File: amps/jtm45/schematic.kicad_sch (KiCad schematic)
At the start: 62 parts, among them T3 OT

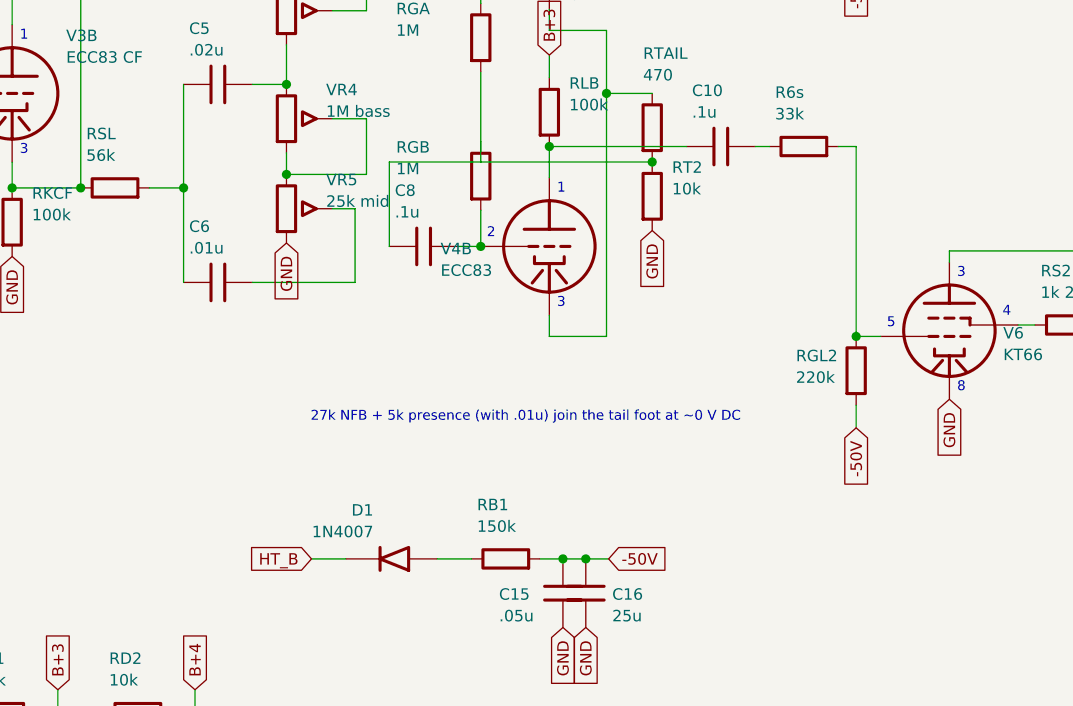
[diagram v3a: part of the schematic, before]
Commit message: Correct Marshall tail returns, tone values and source explanations (#34)
* Fix JTM45 tail return and source-read tone capacitor assignments

Read jtm45tr.gif at 2194x1539: PI/tone crop (1080,250)-(1490,675) shows the 10k tail ending at the feedback/presence junction, bass .01u and middle .02u. Model and draw both DC returns, label the presence parts, reconcile the derived board and retire the incorrect KPI dispute. All twelve chart nodes now pass; KPI 43.048 V vs 40 V, worst deviation 9.7%.

Correct the excluded tremolo description from bias modulation to the V2-driven 2G374 signal shunt; retain the plain head scope. Source: https://www.drtube.com/schematics/marshall/jtm45tr.gif. Both board styles and schematic preview inspected; KiCanvas review remains required at integration.

Signed-off-by: AnalogMaker <theanalogmaker@gmail.com>

* Include JTM100 feedback resistor as a second DC tail return

The 1068x759 factory 1959t-66.gif crop (475,160)-(775,500) shows 27k from the presence junction through the OT secondary, parallel with the 5k track. It is not DC-neutral. Adding RNFB brings PRES from18.092 to15.352 V (chart16) and KPI from55.978 to53.452 V (chart52), with no drawing or claim changes. Correct the explanation and its outdated JTM45 comparison.

Source: https://www.drtube.com/schematics/marshall/1959t-66.gif
Signed-off-by: AnalogMaker <theanalogmaker@gmail.com>

* Restore M1959 presence track and separate feedback tail node

Read Unicord70-6-11 revB from native1377x904 embedded page3 of the cited PDF. Crop(770,165)-(1030,490) grounds the 5k lower lug; 47k feedback and the cold-grid .1u coupler share the tail foot after10k. Crop(1230,210)-(1360,325) resolves feedback at8 ohms, hopping the16-ohm lead. Reconcile model, sheet, board, BOM and prose.

The page2 Mark II drawing has a different4.7k/DC-blocked presence return. Remove the false identical-front-end and chart-proves-grounded-tail claims, retain the printed18.5 V value and report the36.502 V simulation hone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
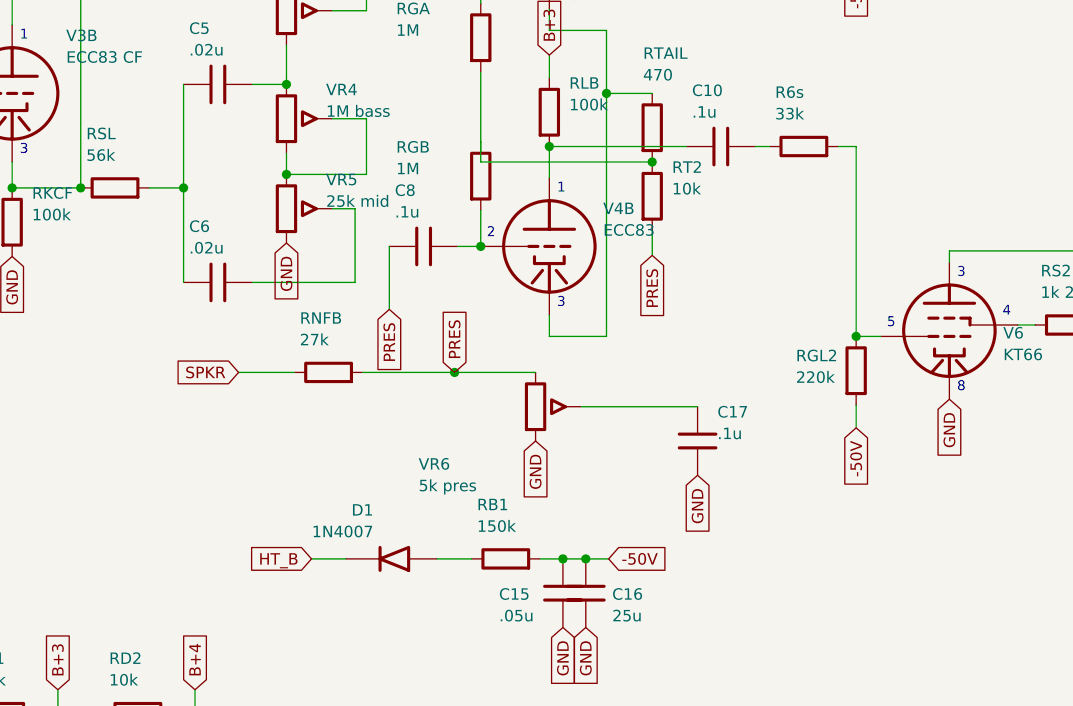
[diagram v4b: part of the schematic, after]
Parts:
- removed C11: 32u, symbol cx:C
- removed C13, C14: 16u, symbol cx:C
- removed RGB: 1M, symbol cx:R
- removed RGL1: 220k, symbol cx:R
- removed RS1: 1k 2W, symbol cx:R
- added C15: .05u, symbol cx:C
- added C17, C8, C9: .1u, symbol cx:C
- added D1: 1N4007, symbol cx:DIODE_SS
- added R6s: 33k, symbol cx:R
- added RB1: 150k, symbol cx:R
- added V6: KT66, symbol cx:PENTODE
- added VR6: 5k pres, symbol cx:POT
- C11: renamed from C12; value 16u -> 32u
- C12: renamed from RD2; value 10k -> 16u; symbol cx:R -> cx:C
- C13: renamed from D1; value 1N4007 -> 16u; symbol cx:DIODE_SS -> cx:C
- C14: renamed from C15; value .05u -> 16u
- C6: value .01u -> .02u
- RD2: renamed from RB1; value 150k -> 10k
- RGB: renamed from C8; value .1u -> 1M; symbol cx:C -> cx:R
- RGL1: renamed from R6s; value 33k -> 220k
- RNFB: renamed from C9; value .1u -> 27k; symbol cx:C -> cx:R
- RS1: renamed from V6; value KT66 -> 1k 2W; symbol cx:PENTODE -> cx:R
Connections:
- net -50V: now also RGL1.2, C15.1, RB1.2; no longer C14.1, RD2.2
- net B+1: now also C11.1
- net B+2: now also C12.1, RS1.2; no longer C11.1
- net B+3: now also C13.1, RD2.1; no longer C12.1
- net B+4: now also C14.1, RD2.2; no longer C12.2
- net GND: now also C12.2, C13.2, C15.2, C17.2, V6.4 (K), VR6.3; no longer RS1.4 (K), RT2.2
- net HT_B: now also D1.2 (K); no longer C13.2 (K)
- net SPKR: now also RNFB.1
- net at RS2.1: now also V6.3 (G2); no longer RS1.3 (G2)
- net at RGB.2, V4B.2 (G): now also C8.2
- net at R5s.2, V5.2 (G1): now also RGL1.1
- net at C10.2: now also R6s.1; no longer RGL1.1
- net at V5.3 (G2): now also RS1.1
- net at RLA.2, V4A.1 (P): now also C9.1; no longer RNFB.1
- net at R5s.1: now also C9.2; no longer RNFB.2
- net at T3.3 (PRI_B): now also V6.1 (P); no longer RS1.1 (P)
- new net: D1.1 (A), RB1.1
- new net: R6s.2, RGL2.1, V6.2 (G1)
- new net: C17.1, VR6.2 (W)
- new net PRES: C8.1, RNFB.2, RT2.2, VR6.1
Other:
- note removed: "27k NFB + 5k presence (with .01u) join the tail foot at ~0 V DC"
- moved on the sheet: C11, C13, C14, RD2, RGL1
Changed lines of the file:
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@@
     (in_bom yes) (on_board yes)
     (property "Reference" "C6" (at 130.109 70.078 270) (effects (font (size 1.27 1.27)) (justify left)))
-    (property "Value" ".01u" (at 130.109 72.478 270) (effects (font (size 1.27 1.27)) (justify left))))
+    (property "Value" ".02u" (at 130.109 72.478 270) (effects (font (size 1.27 1.27)) (justify left))))
   (wire (pts (xy 129.499 76.278) (xy 129.499 76.278))
     (stroke (width 0) (type default)))
@@
   (symbol (lib_id "cx:TRIODE") (at 170.139 72.278 0) (unit 1)
     (in_bom yes) (on_board yes)
-    (property "Reference" "V4B" (at 158.051 72.558 0) (effects (font (size 1.27 1.27)) (justify left)))
-    (property "Value" "ECC83" (at 158.051 74.958 0) (effects (font (size 1.27 1.27)) (justify left))))
+    (property "Reference" "V4B" (at 176.119 68.098 0) (effects (font (size 1.27 1.27)) (justify left)))
+    (property "Value" "ECC83" (at 176.119 70.498 0) (effects (font (size 1.27 1.27)) (justify left))))
   (wire (pts (xy 170.139 30.658) (xy 170.139 27.178))
     (stroke (width 0) (type default)))
@@
     (property "Reference" "RT2" (at 183.769 63.508 0) (effects (font (size 1.27 1.27)) (justify left)))
     (property "Value" "10k" (at 183.769 65.908 0) (effects (font (size 1.27 1.27)) (justify left))))
-  (global_label "GND" (shape input) (at 181.569 70.518 270)
+  (wire (pts (xy 181.569 70.518) (xy 181.569 73.278))
+    (stroke (width 0) (type default)))
+  (global_label "PRES" (shape input) (at 181.569 73.278 270)
     (effects (font (size 1.27 1.27)) (justify right)))
   (wire (pts (xy 162.519 38.278) (xy 162.519 45.278))
@@
   (wire (pts (xy 152.359 72.278) (xy 152.359 72.278))
     (stroke (width 0) (type default)))
-  (wire (pts (xy 152.359 72.278) (xy 152.359 62.898))
+  (wire (pts (xy 152.359 72.278) (xy 152.359 79.278))
     (stroke (width 0) (type default)))
-  (wire (pts (xy 152.359 62.898) (xy 162.519 62.898))
+  (global_label "PRES" (shape input) (at 152.359 79.278 270)
+    (effects (font (size 1.27 1.27)) (justify right)))
+  (global_label "SPKR" (shape input) (at 135.609 86.278 180)
+    (effects (font (size 1.27 1.27)) (justify right)))
+  (wire (pts (xy 135.609 86.278) (xy 141.799 86.278))
     (stroke (width 0) (type default)))
-  (text "27k NFB + 5k presence (with .01u) join the tail foot at ~0 V DC" (at 143.609 91.278 0)
-    (effects (font (size 1.1 1.1)) (justify left)))
+  (symbol (lib_id "cx:R") (at 145.609 86.278 90) (unit 1)
+    (in_bom yes) (on_board yes)
+    (property "Reference" "RNFB" (at 142.409 80.278 270) (effects (font (size 1.27 1.27)) (justify left)))
+    (property "Value" "27k" (at 142.409 82.678 270) (effects (font (size 1.27 1.27)) (justify left))))
+  (wire (pts (xy 149.419 86.278) (xy 159.609 86.278))
+    (stroke (width 0) (type default)))
+  (wire (pts (xy 159.609 86.278) (xy 168.609 86.278))
+    (stroke (width 0) (type default)))
+  (junction (at 159.609 86.278) (diameter 1.02) (color 0 0 0 0))
+  (global_label "PRES" (shape input) (at 159.609 86.278 90)
+    (effects (font (size 1.27 1.27)) (justify left)))
+  (symbol (lib_id "cx:POT") (at 168.609 90.088 0) (unit 1)
+    (in_bom yes) (on_board yes)
+    (property "Reference" "VR6" (at 155.609 96.488 0) (effects (font (size 1.27 1.27)) (justify left)))
+    (property "Value" "5k pres" (at 155.609 98.888 0) (effects (font (size 1.27 1.27)) (justify left))))
+  (global_label "GND" (shape input) (at 168.609 93.898 270)
+    (effects (font (size 1.27 1.27)) (justify right)))
+  (wire (pts (xy 173.689 90.088) (xy 186.609 90.088))
+    (stroke (width 0) (type default)))
+  (symbol (lib_id "cx:C") (at 186.609 93.898 0) (unit 1)
+    (in_bom yes) (on_board yes)
+    (property "Reference" "C17" (at 188.809 90.698 0) (effects (font (size 1.27 1.27)) (justify left)))
+    (property "Value" ".1u" (at 188.809 93.098 0) (effects (font (size 1.27 1.27)) (justify left))))
+  (global_label "GND" (shape input) (at 186.609 97.708 270)
+    (effects (font (size 1.27 1.27)) (justify right)))
   (wire (pts (xy 170.139 27.178) (xy 187.919 27.178))
     (stroke (width 0) (type default)))

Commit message: Fix: the JTM45 drawing has no KT66 grid stoppers; the 33 kΩ pair is removed
V1 source audit (docs/plans/active/2026-10-03-verification-hardening/jtm45.md,
finding F5). On jtm45tr.gif (2194x1539, crop 1590,280,1800,560) each 0.1 PI
coupler lands straight on its KT66 grid node, where the 220K leak also hangs;
there is no resistor in either grid lead. The drawing's only 33K is in the
tremolo depth network (the 10K / 50K / 33K string below the V2 tremolo valve).
meta.yaml cites no other source for the stoppers.

R5s/R6s are removed from the parts list, netlist, sheet and the derived board
(C9/C10 now run to pin 5), and the notes and source description say so. With
no grid current the stoppers dropped nothing: every gated node is unchanged
(BP2 448.7, BP3 380.4, BP4 326.3, KPI 43.0 V).

The audit's other JTM45 findings (V1A load glyph, a cap across the bright
mixer, a PI plate-to-plate cap, the screen network, the OT centre-tap feed and
the bias network) are recorded for a second reader and not changed here.

Co-Authored-By: Claude Opus 5.5 <noreply@anthropic.com>
Claude-Session: https://claude.ai/code/session_01KBMfdh37HmCL2iWcBiL5J1
Signed-off-by: AnalogMaker <theanalogmaker@gmail.com>
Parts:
- removed C15: .05u, symbol cx:C
- removed R5s, R6s: 33k, symbol cx:R
- removed RGL1: 220k, symbol cx:R
- removed V6: KT66, symbol cx:PENTODE
- added C10: .1u, symbol cx:C
- added RD2: 10k, symbol cx:R
- added V5: KT66, symbol cx:PENTODE
- C14: renamed from RD2; value 10k -> 16u; symbol cx:R -> cx:C
- C15: renamed from RB1; value 150k -> .05u; symbol cx:R -> cx:C
- RB1: renamed from C14; value 16u -> 150k; symbol cx:C -> cx:R
- RGL1: renamed from V5; value KT66 -> 220k; symbol cx:PENTODE -> cx:R
- V6: renamed from C10; value .1u -> KT66; symbol cx:C -> cx:PENTODE
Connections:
- net -50V: now also C15.1, RB1.2, RGL1.2; no longer C15.2
- net B+3: now also RD2.1; no longer C14.1
- net B+4: now also C14.1, RD2.2; no longer C14.2, RB1.1
- net GND: now also C14.2, C15.2, V6.4 (K), V5.4 (K); no longer RB1.2, RGL1.4 (K)
- net at D1.1 (A): now also RB1.1; no longer C15.1
- net at T3.3 (PRI_B): now also V6.1 (P)
- net at RGL2.1: now also V6.2 (G1), C10.2
- net at RS2.1: now also V6.3 (G2)
- net at RLB.2, V4B.1 (P): now also C10.1; no longer V6.1
- net at T3.1 (PRI_A): now also V5.1 (P); no longer RGL1.1 (P)
- net at RS1.1: now also V5.3 (G2); no longer RGL1.3 (G2)
- net at C9.2: now also RGL1.1, V5.2 (G1)
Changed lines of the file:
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@@
     (property "Reference" "C9" (at 188.529 20.978 270) (effects (font (size 1.27 1.27)) (justify left)))
     (property "Value" ".1u" (at 188.529 23.378 270) (effects (font (size 1.27 1.27)) (justify left))))
-  (wire (pts (xy 195.539 27.178) (xy 196.609 27.178))
-    (stroke (width 0) (type default)))
-  (symbol (lib_id "cx:R") (at 200.419 27.178 90) (unit 1)
-    (in_bom yes) (on_board yes)
-    (property "Reference" "R5s" (at 197.219 21.178 270) (effects (font (size 1.27 1.27)) (justify left)))
-    (property "Value" "33k" (at 197.219 23.578 270) (effects (font (size 1.27 1.27)) (justify left))))
-  (wire (pts (xy 196.609 27.178) (xy 196.609 27.178))
-    (stroke (width 0) (type default)))
-  (wire (pts (xy 204.229 27.178) (xy 204.229 27.178))
+  (wire (pts (xy 195.539 27.178) (xy 204.229 27.178))
     (stroke (width 0) (type default)))
   (wire (pts (xy 204.229 27.178) (xy 204.229 30.278))
@@
     (property "Reference" "C10" (at 185.989 54.978 270) (effects (font (size 1.27 1.27)) (justify left)))
     (property "Value" ".1u" (at 185.989 57.378 270) (effects (font (size 1.27 1.27)) (justify left))))
-  (wire (pts (xy 192.999 61.178) (xy 194.609 61.178))
-    (stroke (width 0) (type default)))
-  (symbol (lib_id "cx:R") (at 198.419 61.178 90) (unit 1)
-    (in_bom yes) (on_board yes)
-    (property "Reference" "R6s" (at 195.219 55.178 270) (effects (font (size 1.27 1.27)) (justify left)))
-    (property "Value" "33k" (at 195.219 57.578 270) (effects (font (size 1.27 1.27)) (justify left))))
-  (wire (pts (xy 194.609 61.178) (xy 194.609 61.178))
-    (stroke (width 0) (type default)))
-  (wire (pts (xy 202.229 61.178) (xy 204.229 61.178))
+  (wire (pts (xy 192.999 61.178) (xy 204.229 61.178))
     (stroke (width 0) (type default)))
   (wire (pts (xy 204.229 61.178) (xy 204.229 82.278))

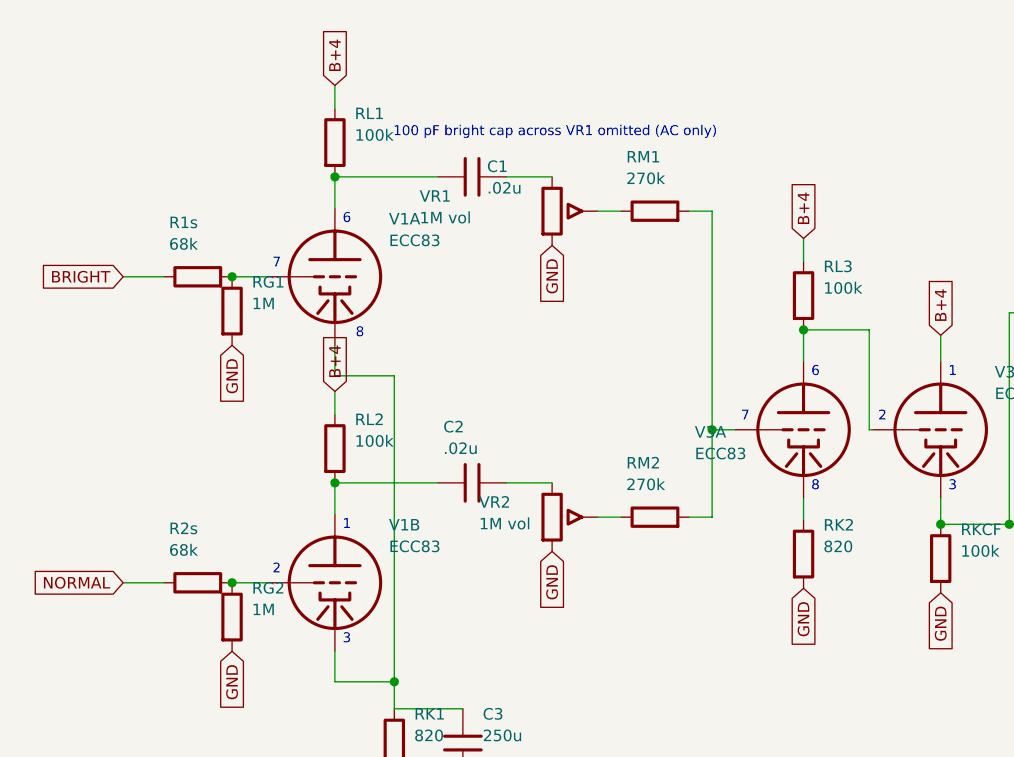
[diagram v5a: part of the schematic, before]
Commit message: Fix: JTM45 bright channel is V1B, as the factory drawing letters it
The drawing's V1A plate feeds the plain 1M volume; V1B's plate (100K load)
feeds the volume carrying the 100 pF, so V1B is the bright channel. The
corpus had the halves swapped. Jack -> grid wiring is unchanged; only the
channel names follow the volumes: BOM roles, sheet labels and the 100 pF
note (now on VR2), board pot and jack labels.

V1A's load is printed "1■0K" with an illegible middle digit (0 or 8). 100K
stays modelled: the chart's equal 220 V plates on a shared cathode falsify
180K. That is recorded in the BOM role and notes as elimination, not a read.

Co-Authored-By: Claude Opus 5.5 <noreply@anthropic.com>
Claude-Session: https://claude.ai/code/session_01KBMfdh37HmCL2iWcBiL5J1
Signed-off-by: AnalogMaker <theanalogmaker@gmail.com>
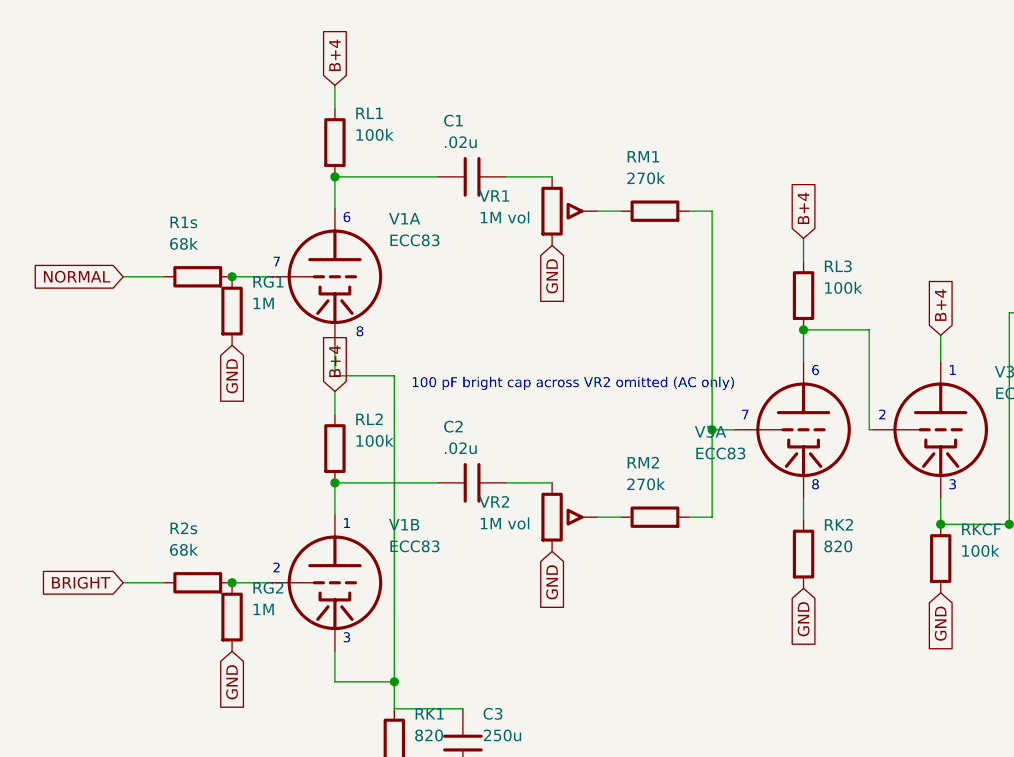
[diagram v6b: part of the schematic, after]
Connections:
- net BRIGHT: now also R2s.1; no longer R1s.1
- net NORMAL: now also R1s.1; no longer R2s.1
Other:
- note added: "100 pF bright cap across VR2 omitted (AC only)"
- note removed: "100 pF bright cap across VR1 omitted (AC only)"
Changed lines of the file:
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@@
     (comment 2 "CC-BY-SA 4.0 · circuitcodex.com")
     (comment 3 "Values read from: https://www.drtube.com/schematics/marshall/jtm45tr.gif"))
-  (global_label "BRIGHT" (shape input) (at 19.6088 38.278 180)
+  (global_label "NORMAL" (shape input) (at 19.6088 38.278 180)
     (effects (font (size 1.27 1.27)) (justify right)))
   (wire (pts (xy 19.6088 38.278) (xy 24.0888 38.278))
@@
   (symbol (lib_id "cx:C") (at 58.3788 27.178 90) (unit 1)
     (in_bom yes) (on_board yes)
-    (property "Reference" "C1" (at 60.0408 26.046 270) (effects (font (size 1.27 1.27)) (justify left)))
-    (property "Value" ".02u" (at 60.0408 28.446 270) (effects (font (size 1.27 1.27)) (justify left))))
+    (property "Reference" "C1" (at 55.1788 20.978 270) (effects (font (size 1.27 1.27)) (justify left)))
+    (property "Value" ".02u" (at 55.1788 23.378 270) (effects (font (size 1.27 1.27)) (justify left))))
   (wire (pts (xy 62.1888 27.178) (xy 67.2688 27.178))
     (stroke (width 0) (type default)))
   (symbol (lib_id "cx:POT") (at 67.2688 30.988 0) (unit 1)
     (in_bom yes) (on_board yes)
-    (property "Reference" "VR1" (at 52.5476 29.348 0) (effects (font (size 1.27 1.27)) (justify left)))
-    (property "Value" "1M vol" (at 52.5476 31.748 0) (effects (font (size 1.27 1.27)) (justify left))))
+    (property "Reference" "VR1" (at 59.1476 29.348 0) (effects (font (size 1.27 1.27)) (justify left)))
+    (property "Value" "1M vol" (at 59.1476 31.748 0) (effects (font (size 1.27 1.27)) (justify left))))
   (global_label "GND" (shape input) (at 67.2688 34.798 270)
     (effects (font (size 1.27 1.27)) (justify right)))
@@
   (wire (pts (xy 85.0488 30.988) (xy 85.0488 55.278))
     (stroke (width 0) (type default)))
-  (global_label "NORMAL" (shape input) (at 19.6088 72.278 180)
+  (global_label "BRIGHT" (shape input) (at 19.6088 72.278 180)
     (effects (font (size 1.27 1.27)) (justify right)))
   (wire (pts (xy 19.6088 72.278) (xy 24.0888 72.278))
@@
     (stroke (width 0) (type default)))
   (junction (at 85.0488 55.278) (diameter 1.02) (color 0 0 0 0))
-  (text "100 pF bright cap across VR1 omitted (AC only)" (at 49.6088 22.278 0)
+  (text "100 pF bright cap across VR2 omitted (AC only)" (at 51.6088 50.278 0)
     (effects (font (size 1.1 1.1)) (justify left)))
   (wire (pts (xy 43.1388 45.898) (xy 43.1388 49.278))
